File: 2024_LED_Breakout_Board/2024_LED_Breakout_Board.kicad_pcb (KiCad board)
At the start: 2 copper layers, 75 x 138 mm, 87 parts, among them J1 43045-1015, J2 43045-1615, J3 43045-2215

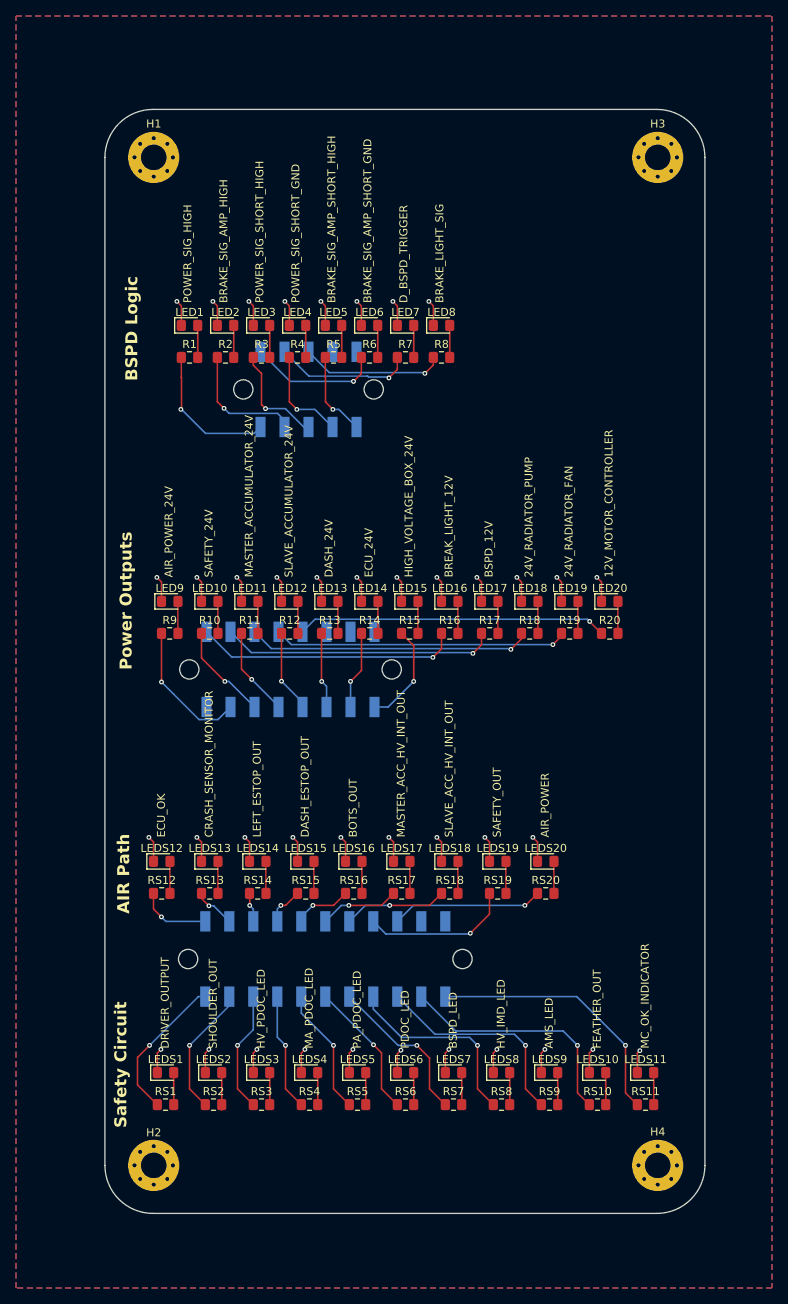
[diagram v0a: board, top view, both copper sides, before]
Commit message: Board resized to 68mm
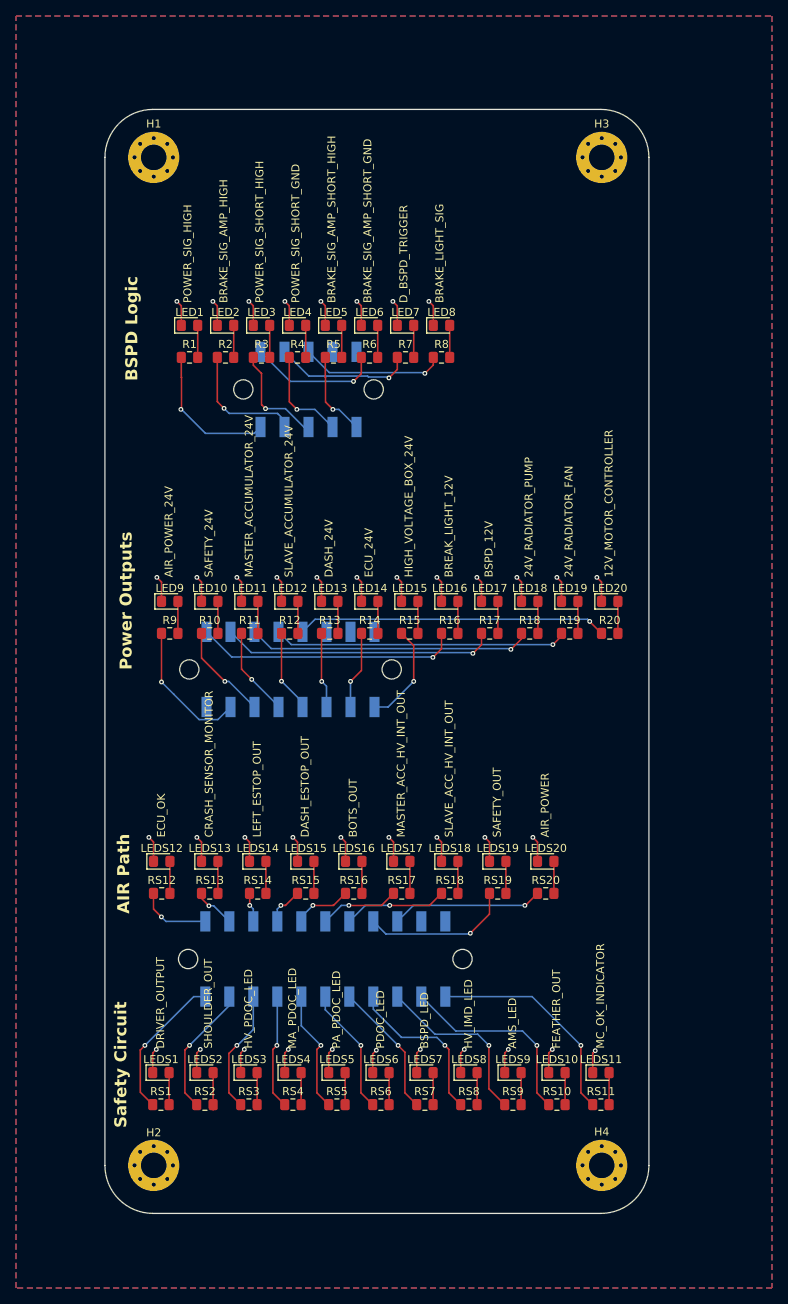
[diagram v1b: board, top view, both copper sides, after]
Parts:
- moved H3 7.00 mm to (186.6, 70.0)
- moved H4 7.00 mm to (186.6, 196.0)
- moved LEDS11 5.57 mm to (186.5, 184.4)
- moved RS11 5.57 mm to (186.5, 188.4)
- moved LEDS10 5.07 mm to (181.0, 184.4)
- moved RS10 5.07 mm to (181.0, 188.4)
- moved LEDS9 4.57 mm to (175.5, 184.4)
- moved RS9 4.57 mm to (175.5, 188.4)
- moved LEDS8 4.07 mm to (170.0, 184.4)
- moved RS8 4.07 mm to (170.0, 188.4)
- moved LEDS7 3.57 mm to (164.5, 184.4)
- moved RS7 3.57 mm to (164.5, 188.4)
- moved LEDS6 3.07 mm to (159.0, 184.4)
- moved RS6 3.07 mm to (159.0, 188.4)
- moved LEDS5 2.57 mm to (153.5, 184.4)
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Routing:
- net /MC_OK_INDICATOR: track 33.1 -> 27.5 mm
- net /FEATHER_OUT: track 30.1 -> 25.0 mm
- net /AMS_LED: track 26.8 -> 22.2 mm
- net /HV_IMD_LED: track 24.7 -> 20.6 mm
- net /BSPD_LED: track 19.8 -> 17.0 mm
- net /PDOC_LED: track 17.2 -> 16.0 mm
- net /SA_PDOC_LED: track 16.0 -> 15.3 mm
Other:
- board size 75 x 138 mm -> 68 x 138 mm
